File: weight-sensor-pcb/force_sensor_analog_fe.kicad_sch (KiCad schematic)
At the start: 34 parts, among them IC2 INA333AIDGKR, IC3 INA333AIDGKR, IC4 INA333AIDGKR, IC5 INA333AIDGKR, J3 Conn_01x04_Socket, J5 Conn_01x04_Socket, J6 Conn_01x04_Socket, J7 Conn_01x04_Socket, U1 OPA333xxD, U2 OPA333xxD, U3 OPA333xxD, U5 OPA333xxD

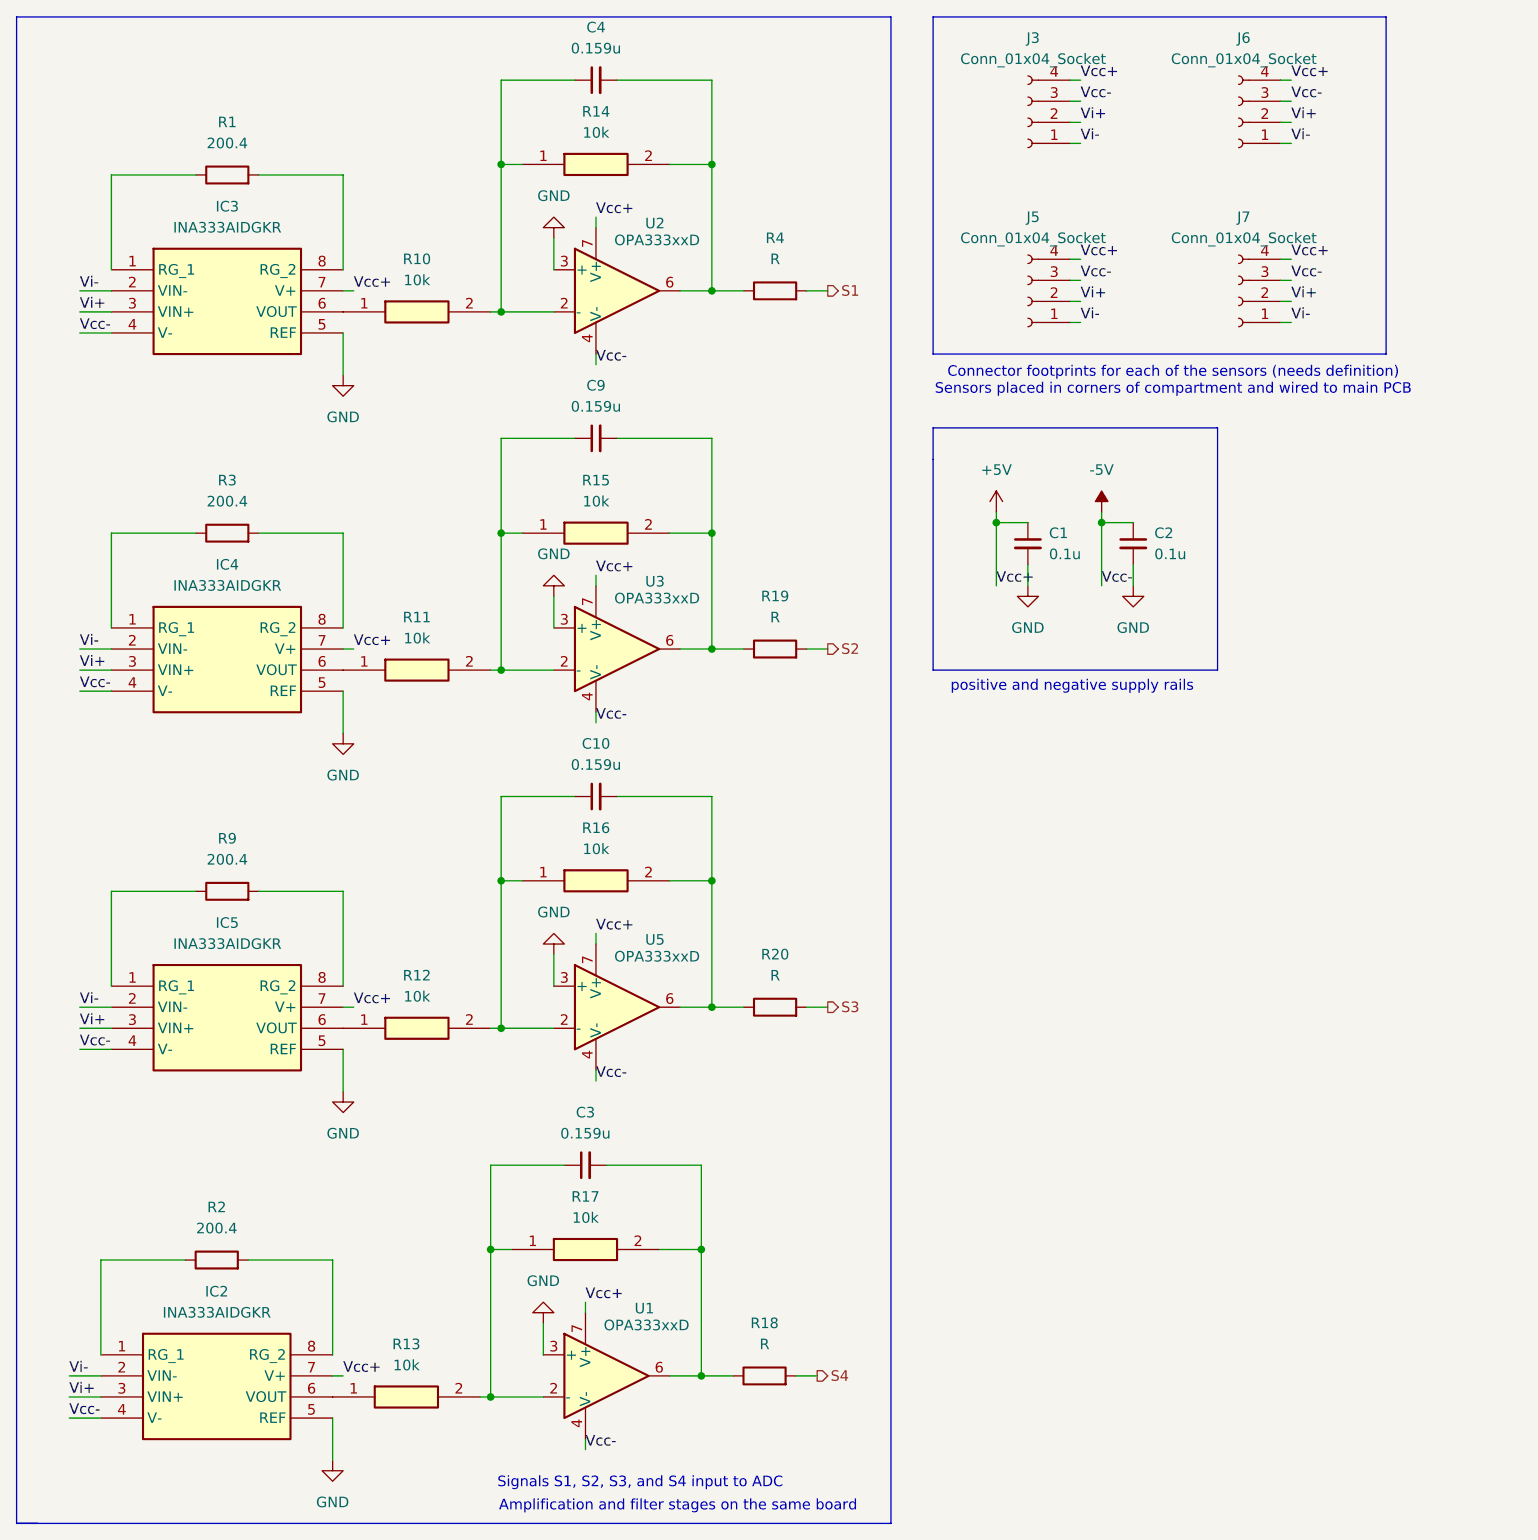
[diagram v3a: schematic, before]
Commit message: add more specific components
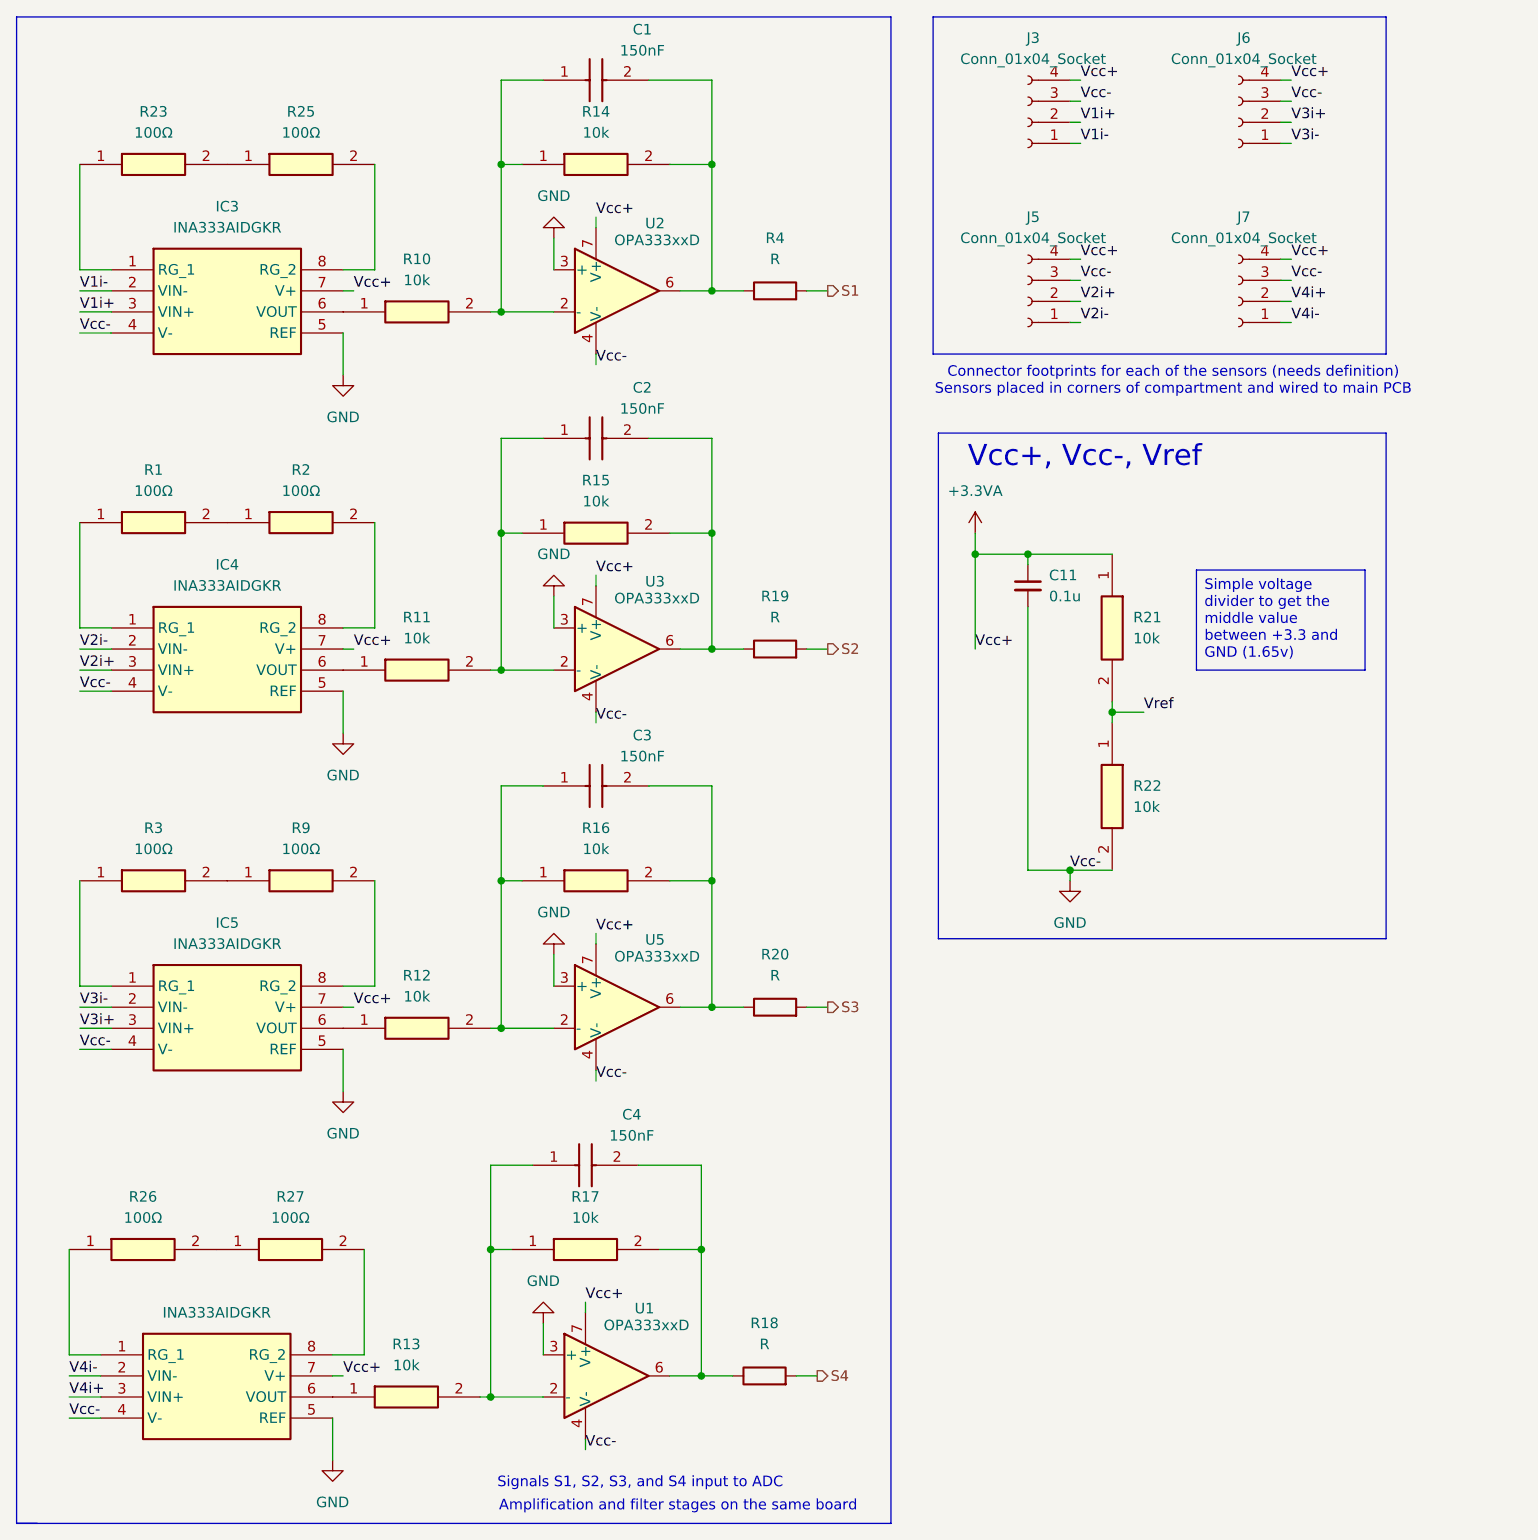
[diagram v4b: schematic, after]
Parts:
- removed C1, C2: 0.1u, symbol Device:C_Small
- removed C10, C3, C4, C9: 0.159u, symbol Device:C_Small
- removed R1, R2, R3, R9: 200.4, symbol Device:R
- added C1, C2, C3, C4: 150nF, C4532_Commercial, symbol Capstone:C4532C0G1H154J250KA
- added C11: 0.1u, symbol Device:C_Small
- added R1, R2, R23, R25, R26, R27, R3, R9: 100Ω, RESC1608X55N, symbol Capstone:RC0603FR-07100RL
- added R21, R22: 10k, RESC1608X55N, symbol Capstone:RMCF0603FT10K0
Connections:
- net -5V is gone; now on net GND: IC2.4 (V-), IC3.4 (V-), IC4.4 (V-), IC5.4 (V-), J3.3 (Pin_3), J5.3 (Pin_3), J6.3 (Pin_3), J7.3 (Pin_3), U1.4 (V-), U2.4 (V-), U3.4 (V-), U5.4 (V-)
- net GND: now also C11.2, R22.2
- net at R11.2, R15.1, U3.2 (-): now also C2.1
- net at R15.2, R19.1, U3.6: now also C2.2
- net at R12.2, R16.1, U5.2 (-): now also C3.1
- net at R16.2, R20.1, U5.6: now also C3.2
- net at IC2.1 (RG_1): now also R26.1
- net at IC2.8 (RG_2): now also R27.2
- net at R17.2, R18.1, U1.6: now also C4.2
- net at IC3.1 (RG_1): now also R23.1
- net at IC3.8 (RG_2): now also R25.2
- net at R10.2, R14.1, U2.2 (-): now also C1.1
- net at R14.2, R4.1, U2.6: now also C1.2
- net at IC5.1 (RG_1): now also R3.1
- net at IC5.8 (RG_2): now also R9.2
- net at IC4.1 (RG_1): now also R1.1
- net at IC4.8 (RG_2): now also R2.2
- net at R13.2, R17.1, U1.2 (-): now also C4.1
- net +5V renamed +3.3VA
- net +3.3VA: now also C11.1, R21.1
- removed net Vi+: IC2.3 (VIN+), IC3.3 (VIN+), IC4.3 (VIN+), IC5.3 (VIN+), J3.2 (Pin_2), J5.2 (Pin_2), J6.2 (Pin_2), J7.2 (Pin_2)
- removed net Vi-: IC2.2 (VIN-), IC3.2 (VIN-), IC4.2 (VIN-), IC5.2 (VIN-), J3.1 (Pin_1), J5.1 (Pin_1), J6.1 (Pin_1), J7.1 (Pin_1)
- new net: R23.2, R25.1
- new net: R26.2, R27.1
- new net: R1.2, R2.1
- new net: R3.2, R9.1
- new net V1i+: IC3.3 (VIN+), J3.2 (Pin_2)
- new net V1i-: IC3.2 (VIN-), J3.1 (Pin_1)
- new net V2i+: IC4.3 (VIN+), J5.2 (Pin_2)
- new net V2i-: IC4.2 (VIN-), J5.1 (Pin_1)
- new net V3i+: IC5.3 (VIN+), J6.2 (Pin_2)
- new net V3i-: IC5.2 (VIN-), J6.1 (Pin_1)
- new net V4i+: IC2.3 (VIN+), J7.2 (Pin_2)
- new net V4i-: IC2.2 (VIN-), J7.1 (Pin_1)
- new net Vref: R21.2, R22.1
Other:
- note added: "Vcc+, Vcc-, Vref"
- note removed: "positive and negative supply rails"

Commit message: started layout
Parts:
- removed C11: 0.1u, symbol Device:C_Small
- removed J3, J5, J6, J7: Conn_01x04_Socket, symbol Connector:Conn_01x04_Socket
- added C9: 0.1uF, CAPC0603X33N, symbol Capstone:GRM033C71C104KE14D
- added J3, J5, J6, J7: SM04B-GHS-TB_LF__SN_, SM04B-GHS-TB, symbol Capstone:SM04B-GHS-TB_LF__SN_
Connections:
- net +3.3VA: now also C9.2, J3.1, J5.1, J6.1, J7.1
- net GND: now also C9.1, J3.4, J5.4, J6.4, J7.4
- net V1i+: now also J3.2
- net V1i-: now also J3.3
- net V2i+: now also J5.2
- net V2i-: now also J5.3
- net V3i+: now also J6.2
- net V3i-: now also J6.3
- net V4i+: now also J7.2
- net V4i-: now also J7.3
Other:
- note added: "Load Cell Connections"

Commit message: layout progress 1
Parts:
- removed R18, R19, R20, R4: R, symbol Device:R
- removed R2, R25, R27, R9: 100Ω, RESC1608X55N, symbol Capstone:RC0603FR-07100RL
- added R18, R2, R4, R9: 0Ω, RESC1608X55N, symbol Capstone:RC0603JR-070RL
- added TP16: Vref, TestPoint:TestPoint_Pad_D1.5mm, symbol Connector:TestPoint
- added TP17: V1 OUT, TestPoint:TestPoint_Pad_D1.5mm, symbol Connector:TestPoint
- added TP18: V2 OUT, TestPoint:TestPoint_Pad_D1.5mm, symbol Connector:TestPoint
- added TP19: V3 OUT, TestPoint:TestPoint_Pad_D1.5mm, symbol Connector:TestPoint
- added TP20: V4 OUT, TestPoint:TestPoint_Pad_D1.5mm, symbol Connector:TestPoint
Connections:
- net GND: no longer IC2.5 (REF), IC3.5 (REF), IC4.5 (REF), IC5.5 (REF), U1.3 (+), U2.3 (+), U3.3 (+), U5.3 (+)
- net S1: now also R2.2
- net S2: now also R4.2
- net S3: now also R9.2
- net S4: now also R18.2
- net Vref: now also IC2.5 (REF), IC3.5 (REF), IC4.5 (REF), IC5.5 (REF), U1.3 (+), U2.3 (+), U3.3 (+), U5.3 (+), TP16.1
- net V2out: now reaches C2.1, R11.2, R15.1, U3.2 (-)
- net V2out: now also TP18.1
- net at C2.2, R15.2, U3.6: now also R4.1
- net at R23.2: now also IC3.8 (RG_2)
- net at R26.2: now also IC2.8 (RG_2)
- net at R1.2: now also IC4.8 (RG_2)
- net at C3.2, R16.2, U5.6: now also R9.1
- net at C4.2, R17.2, U1.6: now also R18.1
- net at R3.2: now also IC5.8 (RG_2)
- net V1out: now reaches C1.1, R10.2, R14.1, U2.2 (-)
- net V1out: now also TP17.1
- net at C1.2, R14.2, U2.6: now also R2.1
- net V3out: now reaches C3.1, R12.2, R16.1, U5.2 (-)
- net V3out: now also TP19.1
- net V4out: now reaches C4.1, R13.2, R17.1, U1.2 (-)
- net V4out: now also TP20.1
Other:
- note added: "0603"
- note added: "Test Points"
- moved on the sheet: C1, C2, C3, C4, IC3, IC4, IC5, R1, R14, R15, R16, R17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

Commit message: Layout draft complete
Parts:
- removed R21, R22: 10k, RESC1608X55N, symbol Capstone:RMCF0603FT10K0
- added C6: 0.1uF, CAPC0603X33N, symbol Capstone:GRM033C71C104KE14D
- added R5, R6, R7, R8: 100Ω, RESC1608X55N, symbol Capstone:RC0603FR-07100RL
- renumbered C4 to C1, C1 to C2, C2 to C3, C3 to C4, C9 to C5, IC2 to IC1, IC3 to IC2, IC4 to IC3, IC5 to IC4, J3 to J1, J5 to J2, J6 to J3, J7 to J4, R26 to R1, R17 to R13, R2 to R17, R4 to R18, R9 to R19, R23 to R2, R18 to R20, R1 to R3, R3 to R4, R13 to R9, TP16 to TP1, TP17 to TP2, TP18 to TP3, TP19 to TP4, TP20 to TP5, U5 to U4
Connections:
- net Vref is gone; now on net GND: IC1.5 (REF), IC2.5 (REF), IC3.5 (REF), IC4.5 (REF), TP1.1, U1.3 (+), U2.3 (+), U3.3 (+), U4.3 (+)
- net GND: now also C6.1; no longer IC1.4 (V-), IC2.4 (V-), IC3.4 (V-), IC4.4 (V-), J1.4, J2.4, J3.4, J4.4, U1.4 (V-), U2.4 (V-), U3.4 (V-), U4.4 (V-)
- net V1i+: now also J1.3; no longer J1.2
- net V1i-: now also J1.2; no longer J1.3
- net V2i+: now also J2.3; no longer J2.2
- net V2i-: now also J2.2; no longer J2.3
- net V3i+: now also J3.3; no longer J3.2
- net V3i-: now also J3.2; no longer J3.3
- net V4i+: now also J4.3; no longer J4.2
- net V4i-: now also J4.2; no longer J4.3
- net at R2.2: now also R6.1; no longer IC2.8 (RG_2)
- net at IC1.8 (RG_2): now also R5.2; no longer R1.2
- net at R4.2: now also R8.1; no longer IC4.8 (RG_2)
- net at R3.2: now also R7.1; no longer IC3.8 (RG_2)
- new net: IC3.8 (RG_2), R7.2
- new net: R1.2, R5.1
- new net: IC2.8 (RG_2), R6.2
- new net: IC4.8 (RG_2), R8.2
- new net -3V3: C6.2, IC1.4 (V-), IC2.4 (V-), IC3.4 (V-), IC4.4 (V-), J1.4, J2.4, J3.4, J4.4, U1.4 (V-), U2.4 (V-), U3.4 (V-), U4.4 (V-)
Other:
- moved on the sheet: R1, R2, R3, R4, TP1, TP2, TP3, TP4, TP5
